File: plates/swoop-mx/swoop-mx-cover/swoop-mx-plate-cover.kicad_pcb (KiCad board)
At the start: 2 copper layers, 18.8 x 54.8 mm, 5 parts

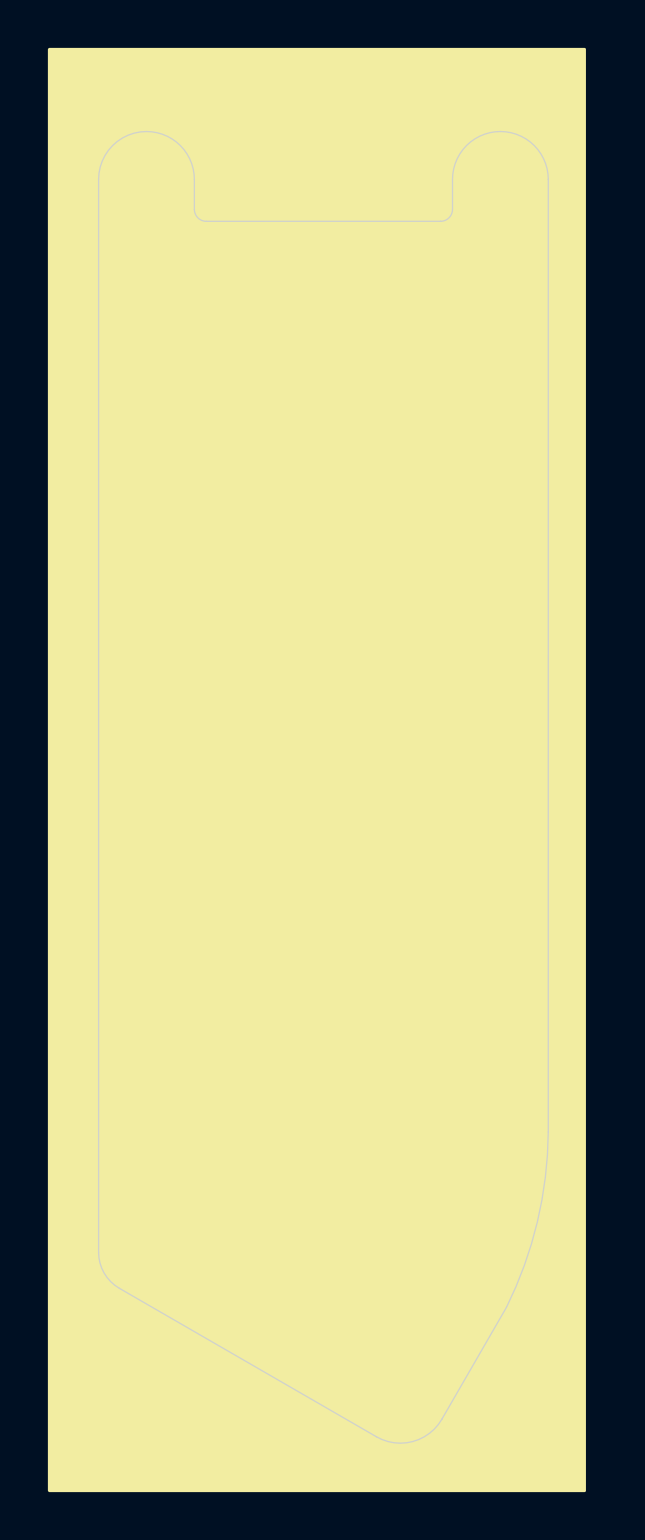
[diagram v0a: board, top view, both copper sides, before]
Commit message: Solid instead of hatch fill on plates.
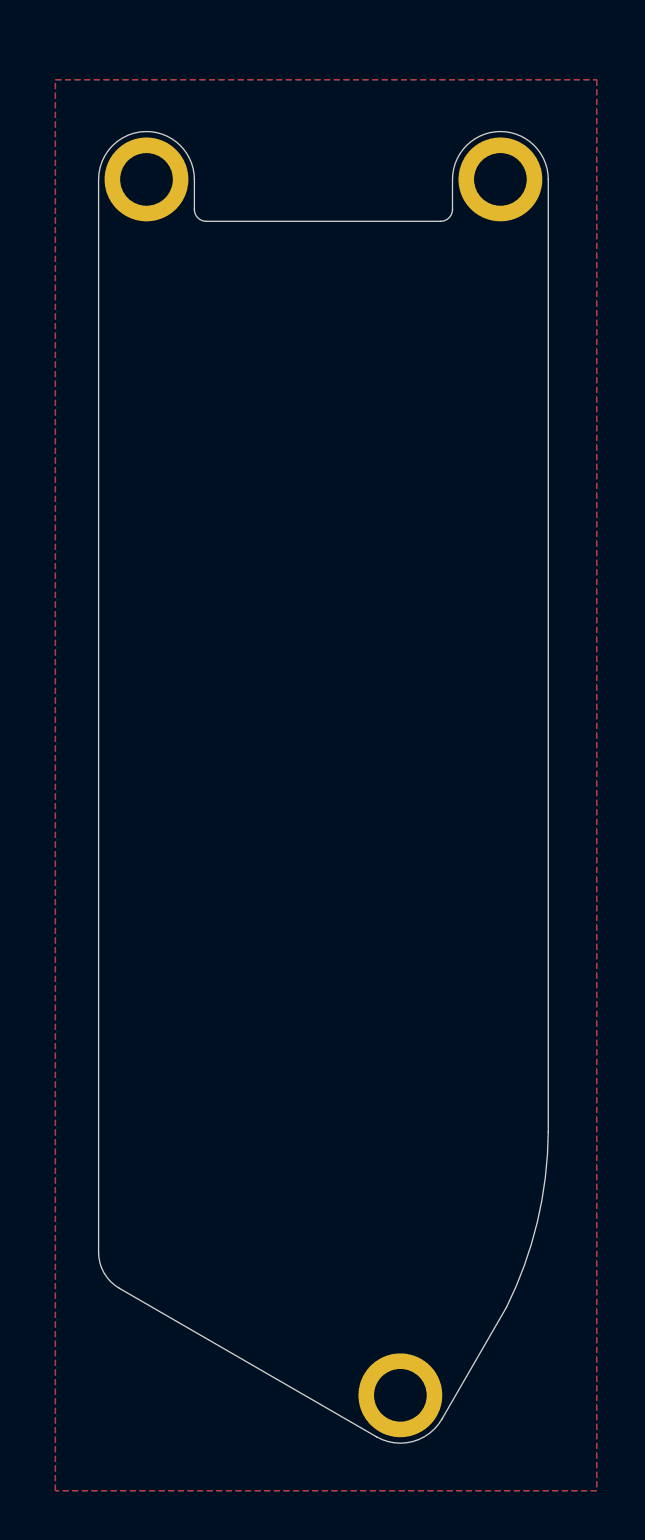
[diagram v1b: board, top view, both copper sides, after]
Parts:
- removed G***: LOGO, chocolad-art:title-bluebell
- removed G***: LOGO, chocolad-art:bluebell
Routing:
- added copper zone on B.Cu, net (none)
- added copper zone on F.Cu, net (none)
